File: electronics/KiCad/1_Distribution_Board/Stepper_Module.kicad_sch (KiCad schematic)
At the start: 8 parts, among them J23 JST PH, J24 Generic 2.54mm, P1 Header-Female-2.54_1x8, P2 Header-Female-2.54_1x2, P3 Header-Female-2.54_1x8

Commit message: distribution board v1.5: re-layout on a 100 x 74 mm board
- outline 100 x 74 mm with the Orange Pi 5 mounting hole pattern, holes non-plated
- drivers A2 to A5 in a row along the top edge, A6 beside the Pico; every
  motor gets both a JST PH plug and a 2.54 mm header
- Pico pins reassigned so step, dir, DIAG, EN, UART0 and the two LED lines
  leave as one ordered bus under the drivers (new hwcfg needed for this rev)
- MS1/MS2 address straps through resistors: A2..A5 are 0..3 on UART0,
  A6 is 0 on UART1
- removed the 12 V and servo-voltage outputs and the second servo connector
  that carried 24 V on its power pin
- each rail runs regulator, cap, test point, indicator LED in one column
- silkscreen says what every connector is for: 24V IN, SERIAL SERVO (D, V+, G),
  LED1 to LED4, HALL, RESET, driver names and their EN corner
- GND poured on both layers and stitched; DRC clean, nothing unconnected

Co-Authored-By: Claude Opus 5.5 <noreply@anthropic.com>
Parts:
- added R91, R92: 10kΩ, PCM_JLCPCB:R_0603, symbol PCM_JLCPCB-Resistors:0603,10kΩ
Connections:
- net MS1: now also R91.1; no longer A2.15 (MS1), P1.2
- net MS2: now also R92.1; no longer A2.14 (MS2), P1.3
- new net MS1_PIN: A2.15 (MS1), P1.2, R91.2
- new net MS2_PIN: A2.14 (MS2), P1.3, R92.2

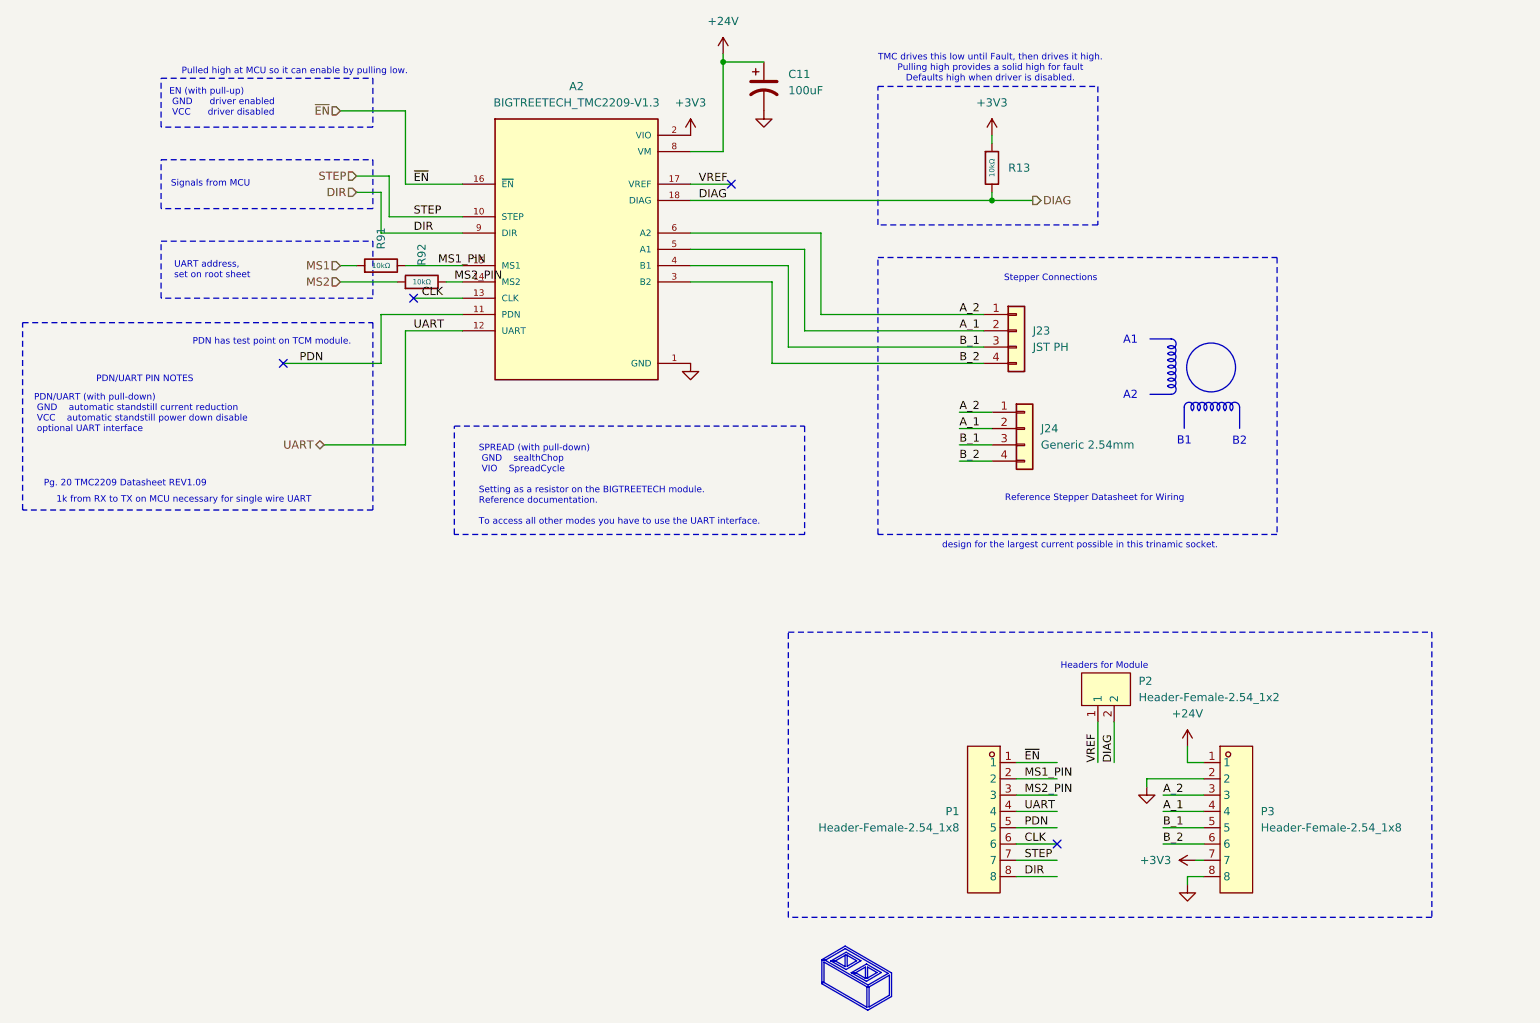
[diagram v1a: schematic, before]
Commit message: distribution board v1.5: orange pi 5 hat link, input protection, review fixes
Mounting and the Pi link:
- The four mounting holes follow the Orange Pi 5's own pattern, 93.86 x 55.89 mm,
  taken from the vendor's STEP model.
- J41 is a 2x9 female socket under the board. It plugs onto pins 1-18 of the Pi's
  26-pin header, at the position measured from the vendor's photos against those
  holes.
- The Pi's USB/Ethernet stack is 16.2 mm tall, so the board stands on M2.5 x 20 mm
  standoffs. J41 is therefore hand-fitted, with a 15-17 mm body (DNP for assembly).
- New Pi_Link sheet. The UART crosses an ISO7721 isolator: Pi UART0_M2 on pins 8
  and 10, Pico PIO UART with GP7 TX and GP19 RX.
- Reset crosses an LTV-357T optocoupler: Pi pin 15 pulls RUN low.
- The Pi's ground stays on its side of the isolators, poured 1 mm clear of the
  board's ground.

Input:
- No fuse in the ground leg: F2 is gone.
- Q7 (AO4485 P-FET) blocks a reversed input, replacing the shunt diode D2.
- D10 (SMBJ26A) clamps surges.
- Input copper is sized for the 10 A fuse, with six vias onto the 24 V bus and
  four onto the LED lane.

Driver sockets:
- CLK (pin 6) to GND.
- PDN (pin 5) joined to UART (pin 4): modules bring PDN_UART out on either pin.

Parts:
- J1 takes the B2P-VH footprint of the part ordered, C160315.
- U3 and U4 carry the R-78K modules that are fitted.

Layout:
- 3V3 crosses above the Pico on the back.
- The reset button sits beside the Pico.
- Driver names sit between their sockets.

Co-Authored-By: Claude Opus 5.5 <noreply@anthropic.com>
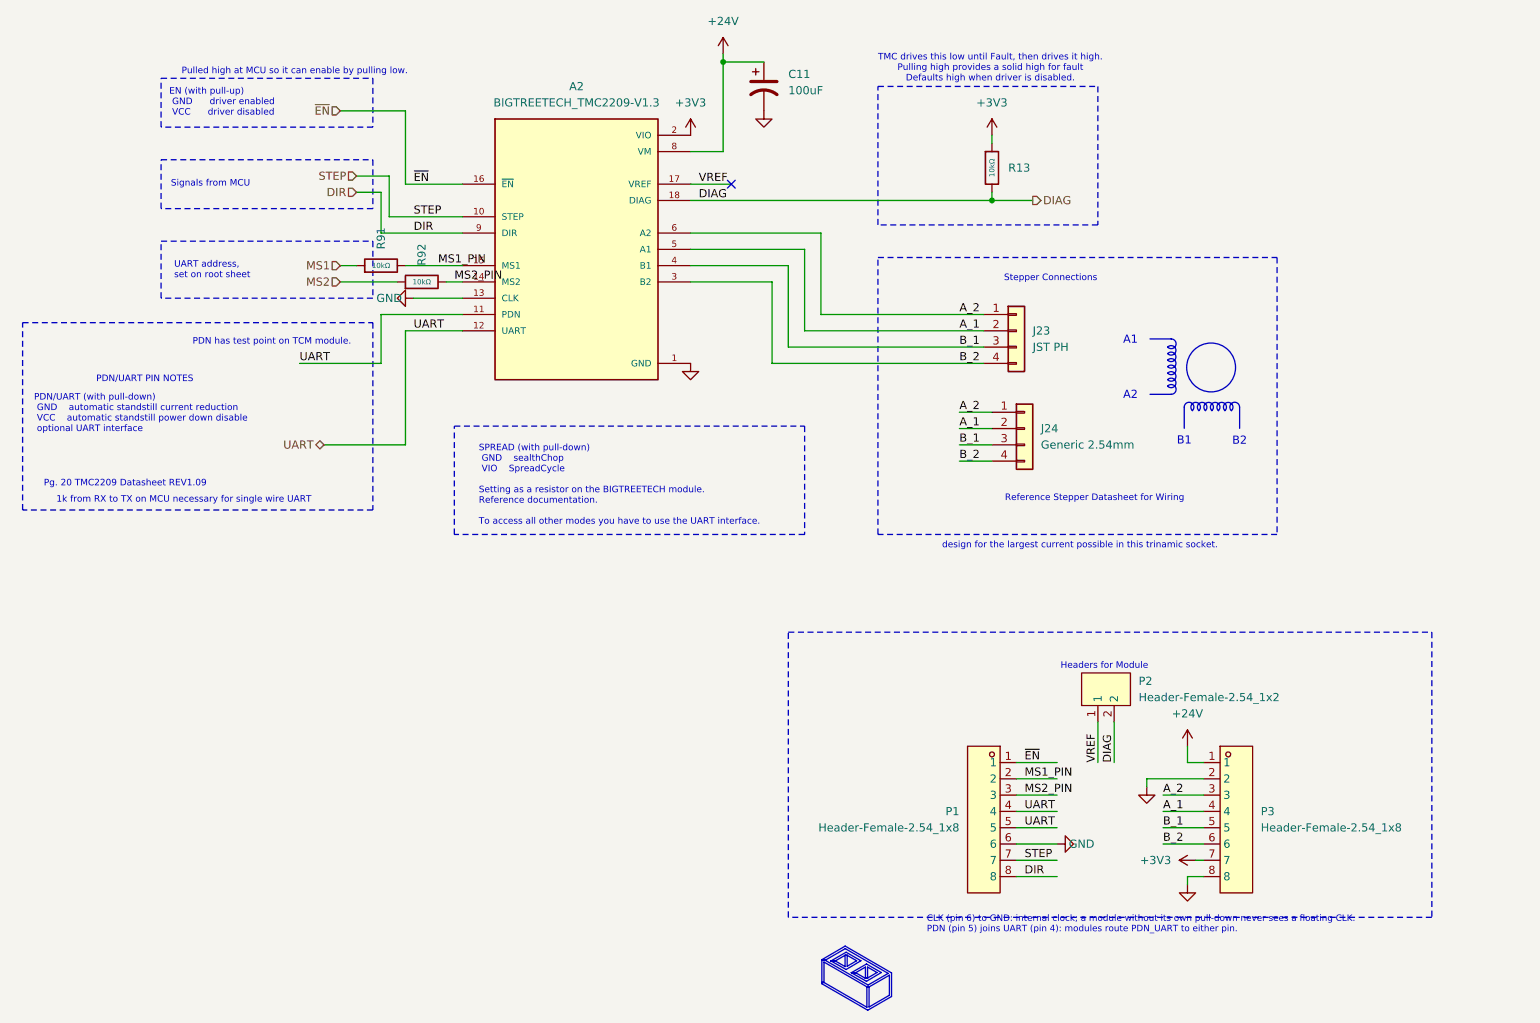
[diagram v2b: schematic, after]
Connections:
- net CLK is gone; now on net GND: A2.13 (CLK), P1.6
- net PDN is gone; now on net UART: A2.11 (PDN), P1.5
- no-connect marks 4 -> 1
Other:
- note added: "CLK (pin 6) to GND: internal clock; a module without its own pull-down never sees a floating CLK. PDN (pin 5) joins UART (pin 4): modules route PDN_UART to either pin."
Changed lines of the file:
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@@
 		(at 165.1 48.26)
 	)
-	(no_connect
-		(at 115.57 66.04)
-	)
-	(no_connect
-		(at 95.25 76.2)
-	)
-	(no_connect
-		(at 215.9 151.13)
-	)
 	(wire
 		(pts
@@
 	(wire
 		(pts
-			(xy 95.25 76.2) (xy 110.49 76.2)
-		)
-		(stroke
-			(width 0)
-			(type default)
-		)
-	)
-	(wire
-		(pts
 			(xy 229.87 140.97) (xy 238.76 140.97)
 		)
@@
 		)
 	)
-	(label "PDN"
+	(label "UART"
 		(at 210.82 148.59 0)
 		(effects
@@
 		)
 	)
-	(label "CLK"
-		(at 210.82 151.13 0)
-		(effects
-			(font
-				(size 1.27 1.27)
-			)
-			(justify left bottom)
-		)
-	)
-	(label "PDN"
+	(label "UART"
 		(at 97.79 76.2 0)
 		(effects
@@
 		)
 	)
-	(label "CLK"
-		(at 116.84 66.04 0)
-		(effects
-			(font
-				(size 1.27 1.27)
-			)
-			(justify left bottom)
-		)
-	)
 	(label "DIR"
 		(at 210.82 156.21 0)
@@
 			)
 			(justify left bottom)
+		)
+	)
+	(symbol
+		(lib_id "power:GND")
+		(at 215.9 151.13 90)
+		(unit 1)
+		(body_style 1)
+		(exclude_from_sim no)
+		(in_bom yes)
+		(on_board yes)
+		(in_pos_files yes)
+		(dnp no)
+		(property "Reference" "#PWR0310"
+			(at 218.44 149.85999999999999 90)
+			(hide yes)
+			(effects
+				(font
+					(size 1.27 1.27)
+				)
+			)
+		)
+		(property "Value" "GND"
+			(at 219.71 151.13 90)
+			(effects
+				(font
+					(size 1.27 1.27)
+				)
+			)
+		)
+		(property "Footprint" ""
+			(at 215.9 151.13 0)
+			(hide yes)
+			(effects
+				(font
+					(size 1.27 1.27)
+				)
+			)
+		)
+		(property "Datasheet" ""
+			(at 215.9 151.13 0)
+			(hide yes)
+			(effects
+				(font
+					(size 1.27 1.27)
+				)
+			)
+		)
+		(property "Description" ""
+			(at 215.9 151.13 0)
+			(hide yes)
+			(effects
+				(font
+					(size 1.27 1.27)
+				)
+			)
+		)
+		(instances
+			(project "1_Distribution_Board"
+				(path "/d53c8c01-e754-4310-8a73-7d7c95e64cd3/02dc68e7-469d-4169-b9e6-1742ced64b14"
+					(reference "#PWR0310")
+					(unit 1)
+				)
+				(path "/d53c8c01-e754-4310-8a73-7d7c95e64cd3/22523adc-9142-4362-af29-41502b0f3187"
+					(reference "#PWR0311")
+					(unit 1)
+				)
+				(path "/d53c8c01-e754-4310-8a73-7d7c95e64cd3/7a480abb-9b9a-47ac-a44b-24d5185d46e0"
+					(reference "#PWR0312")
+					(unit 1)
+				)
+				(path "/d53c8c01-e754-4310-8a73-7d7c95e64cd3/be0591dd-6b80-4d9a-a31b-18ff19c250bb"
+					(reference "#PWR0313")
+					(unit 1)
+				)
+				(path "/d53c8c01-e754-4310-8a73-7d7c95e64cd3/ec0756a4-872d-4fc6-b758-9ad2624703a8"
+					(reference "#PWR0314")
+					(unit 1)
+				)
+			)
+		)
+	)
+	(symbol
+		(lib_id "power:GND")
+		(at 115.57 66.04 270)
+		(unit 1)
+		(body_style 1)
+		(exclude_from_sim no)
+		(in_bom yes)
+		(on_board yes)
+		(in_pos_files yes)
+		(dnp no)
+		(property "Reference" "#PWR0320"
+			(at 118.11 64.77000000000001 270)
+			(hide yes)
+			(effects
+				(font
+					(size 1.27 1.27)
+				)
+			)
+		)
+		(property "Value" "GND"
+			(at 111.76 66.04 270)
+			(effects
+				(font
+					(size 1.27 1.27)
+				)
+			)
+		)
+		(property "Footprint" ""
+			(at 115.57 66.04 0)
+			(hide yes)
+			(effects
+				(font
+					(size 1.27 1.27)
+				)
+			)
+		)
+		(property "Datasheet" ""
+			(at 115.57 66.04 0)
+			(hide yes)
+			(effects
+				(font
+					(size 1.27 1.27)
+				)
+			)
+		)
+		(property "Description" ""
+			(at 115.57 66.04 0)
+			(hide yes)
+			(effects
+				(font
+					(size 1.27 1.27)
+				)
+			)
+		)
+		(instances
+			(project "1_Distribution_Board"
+				(path "/d53c8c01-e754-4310-8a73-7d7c95e64cd3/02dc68e7-469d-4169-b9e6-1742ced64b14"
+					(reference "#PWR0320")
+					(unit 1)
+				)
+				(path "/d53c8c01-e754-4310-8a73-7d7c95e64cd3/22523adc-9142-4362-af29-41502b0f3187"
+					(reference "#PWR0321")
+					(unit 1)
+				)
+				(path "/d53c8c01-e754-4310-8a73-7d7c95e64cd3/7a480abb-9b9a-47ac-a44b-24d5185d46e0"
+					(reference "#PWR0322")
+					(unit 1)
+				)
+				(path "/d53c8c01-e754-4310-8a73-7d7c95e64cd3/be0591dd-6b80-4d9a-a31b-18ff19c250bb"
+					(reference "#PWR0323")
+					(unit 1)
+				)
+				(path "/d53c8c01-e754-4310-8a73-7d7c95e64cd3/ec0756a4-872d-4fc6-b758-9ad2624703a8"
+					(reference "#PWR0324")
+					(unit 1)
+				)
+			)
+		)
+	)
+	(wire
+		(pts
+			(xy 97.79 76.2) (xy 110.49 76.2)
+		)
+		(stroke
+			(width 0)
+			(type default)
+		)
+	)
+	(text "CLK (pin 6) to GND: internal clock; a module without its own pull-down never sees a floating CLK.\nPDN (pin 5) joins UART (pin 4): modules route PDN_UART to either pin."
+		(exclude_from_sim no)
+		(at 195.58 165.1 0)
+		(effects
+			(font
+				(size 1.0 1.0)
+			)
+			(justify left bottom)

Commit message: distribution board v1.5: LED port clamps, GP7 pull-up, low-ESR bulk caps
- D12-D15 (BAS316) from each LED port's switched side to +24V, so an
  inductive load (a fan, a long lead) cannot push the 30 V AO3400A
  switches past their rating at turn-off. A silicon diode rather than a
  Schottky: these sit at 24 V reverse whenever their port is on, and a
  small Schottky's leakage can heat it into thermal runaway. BAS316 is
  rated 30 uA at 25 V with a 150 C junction.
- R105 (10k) pulls GP7, the Pico's TX to the Pi through the isolator, up
  to 3.3 V. The RP2040 holds its pins low through reset, which reached
  the Pi's RX as a break.
- C11-C15 become Panasonic EEE-FT1V101AP (0.26 ohm ESR and 300 mA ripple
  at 100 kHz) on the same footprint; the previous part gave no ESR.
- The isolated ground island ends 0.25 mm sooner, so the Pi side keeps
  1 mm from the board's copper (it was 0.88 mm at J36), with one via to
  keep the island's front fill joined.
- GP19 under U8 moves to the back layer so U8's ground pin stays joined
  to the pour.
- D11-D15 silkscreen lines are 0.15 mm.

Co-Authored-By: Claude Opus 5.5 <noreply@anthropic.com>
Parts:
- C11: LCSC C2836442 -> C128464
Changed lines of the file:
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@@
 			)
 		)
-		(property "Description" "Polarized capacitor, US symbol"
+		(property "Description" "Panasonic EEE-FT1V101AP, 100uF 35V, 260 mohm and 300 mA at 100 kHz"
 			(at 170.18 33.02 0)
 			(hide yes)
@@
 			)
 		)
-		(property "LCSC" "C2836442"
+		(property "LCSC" "C128464"
 			(at 170.18 33.02 0)
 			(hide yes)
